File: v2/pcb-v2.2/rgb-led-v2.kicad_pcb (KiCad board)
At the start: 2 copper layers, 90 x 50 mm, 22 parts, among them CON1 BARREL_JACK, P1 CONN_01X15, P2 CONN_01X15, SW1 SPST

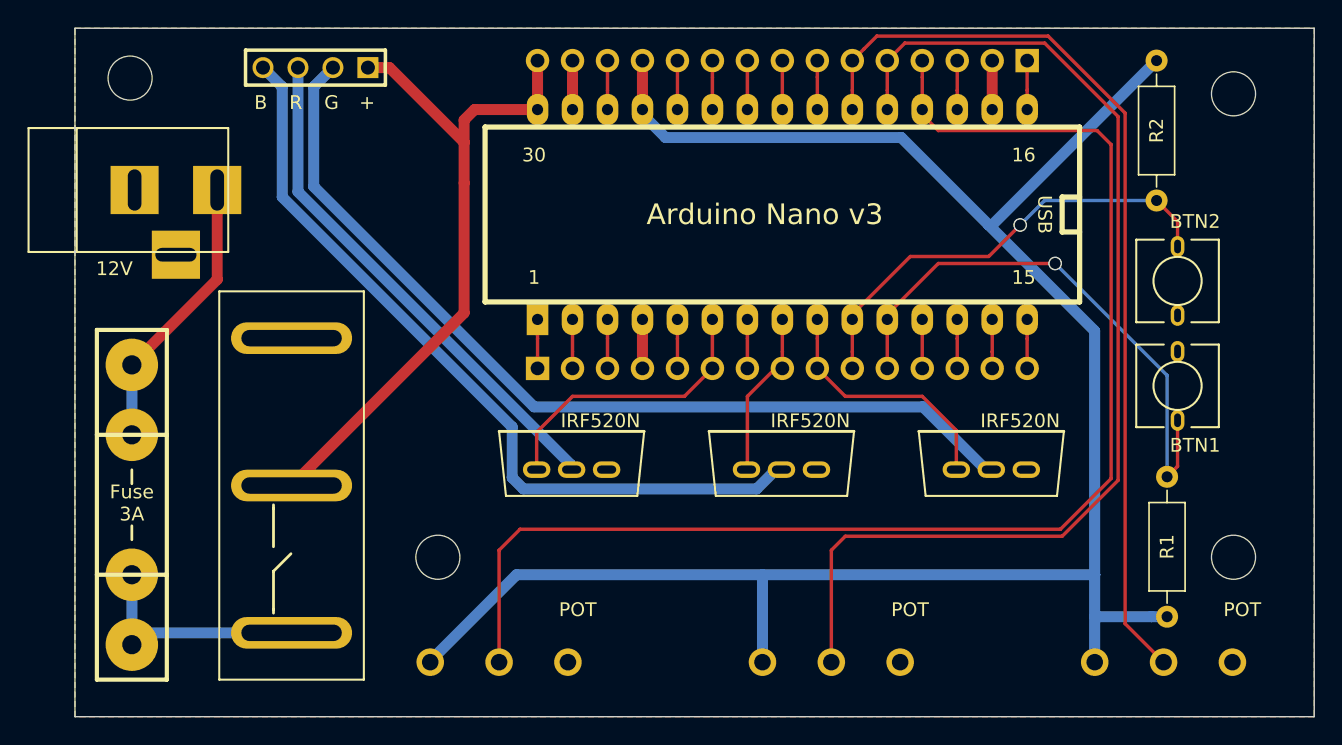
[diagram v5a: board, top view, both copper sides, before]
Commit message: More spacing between pin headers and Arduino
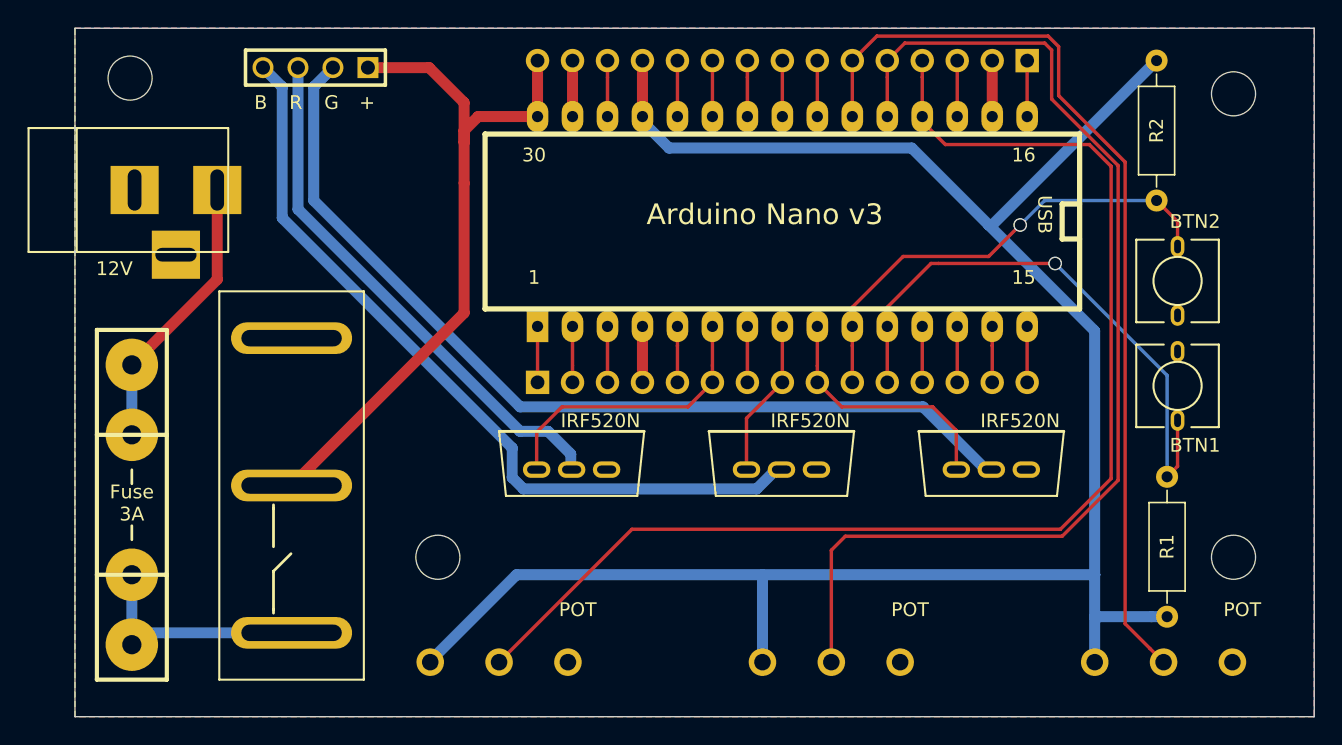
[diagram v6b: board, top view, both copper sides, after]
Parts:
- moved P2 1.02 mm to (52.3, 45.7)
- moved UC1 0.51 mm to (68.8, 34.0)
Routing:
- net A4: track 97.5 -> 92.1 mm
- net VIN: track 50.2 -> 51.7 mm
- net A25: track 33.4 -> 34.7 mm
- net A26: track 40.9 -> 42.2 mm
- net Net-(CONN1-Pad3): track 37.8 -> 39.0 mm
- net GND: track 7.11 -> 8.13 mm
- net A23: track 12.3 -> 11.6 mm
- net Net-(CONN1-Pad2): track 67.0 -> 67.6 mm
- net A6: track 67.5 -> 68.0 mm
- net A30: track 3.56 -> 4.06 mm
- net A29: track 3.56 -> 4.06 mm
- net A28: track 3.56 -> 4.06 mm
- net A27: track 3.56 -> 4.06 mm
- net A22: track 3.56 -> 4.06 mm
- net A20: track 3.56 -> 4.06 mm
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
